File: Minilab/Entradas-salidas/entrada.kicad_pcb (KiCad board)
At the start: 2 copper layers, 140.6 x 50.8 mm, 82 parts, among them J1 Out 5V/0V, J10 Vin, J11 Vin, J12 Vin, J13 Vin, J15 Vin, J16 Vin, J17 VCC, J18 OUT, J19 GND, J2 Out 5V/0V, J20 Conn_01x08_Pin, J21 Conn_01x08_Pin, J3 Out 5V/0V, J4 Out 5V/0V, J5 Out 5V/0V, J6 Out 5V/0V, J7 Vin, J8 Vin, J9 Vin, SW1 SW_SPST, SW2 SW_SPST, SW3 SW_SPST, SW4 SW_SPST, SW5 SW_SPST, SW6 SW_SPST, U1 4049, U10 NE555P, U2 Mini360

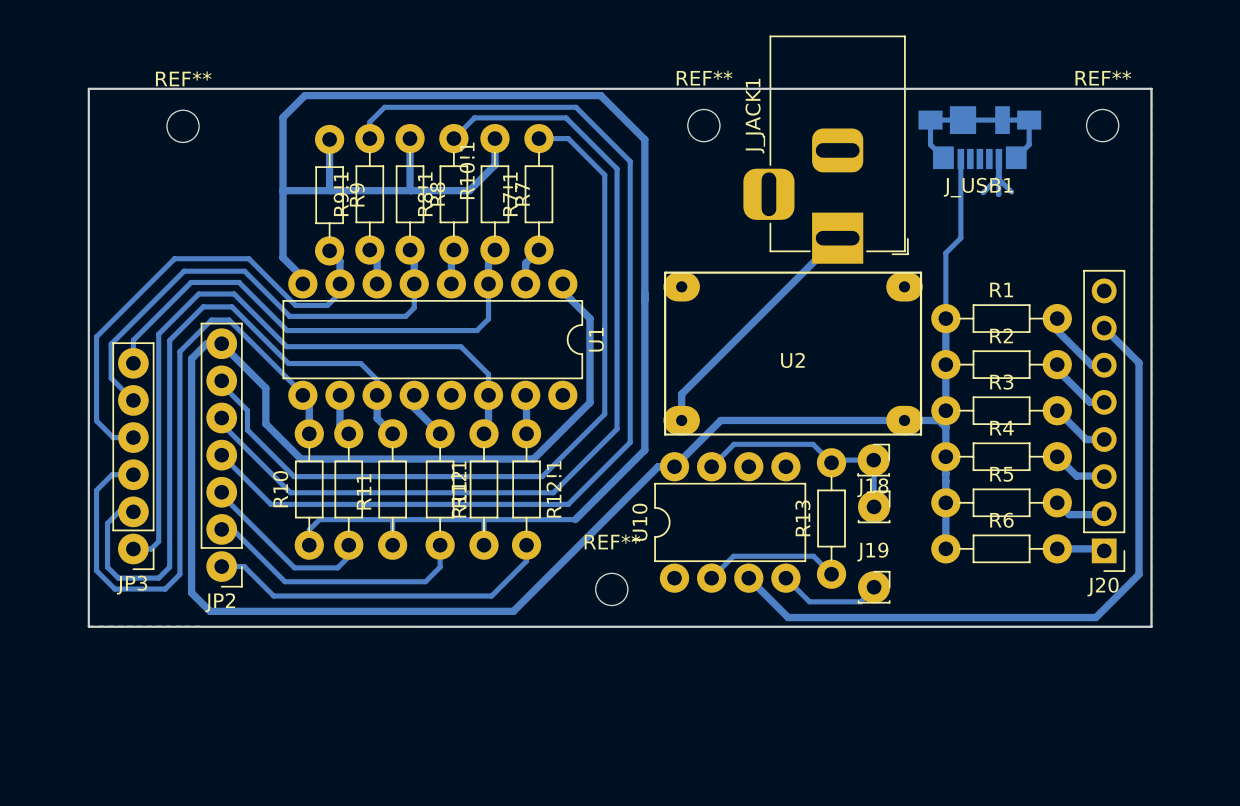
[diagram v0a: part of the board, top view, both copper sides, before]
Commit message: cambio oscilador
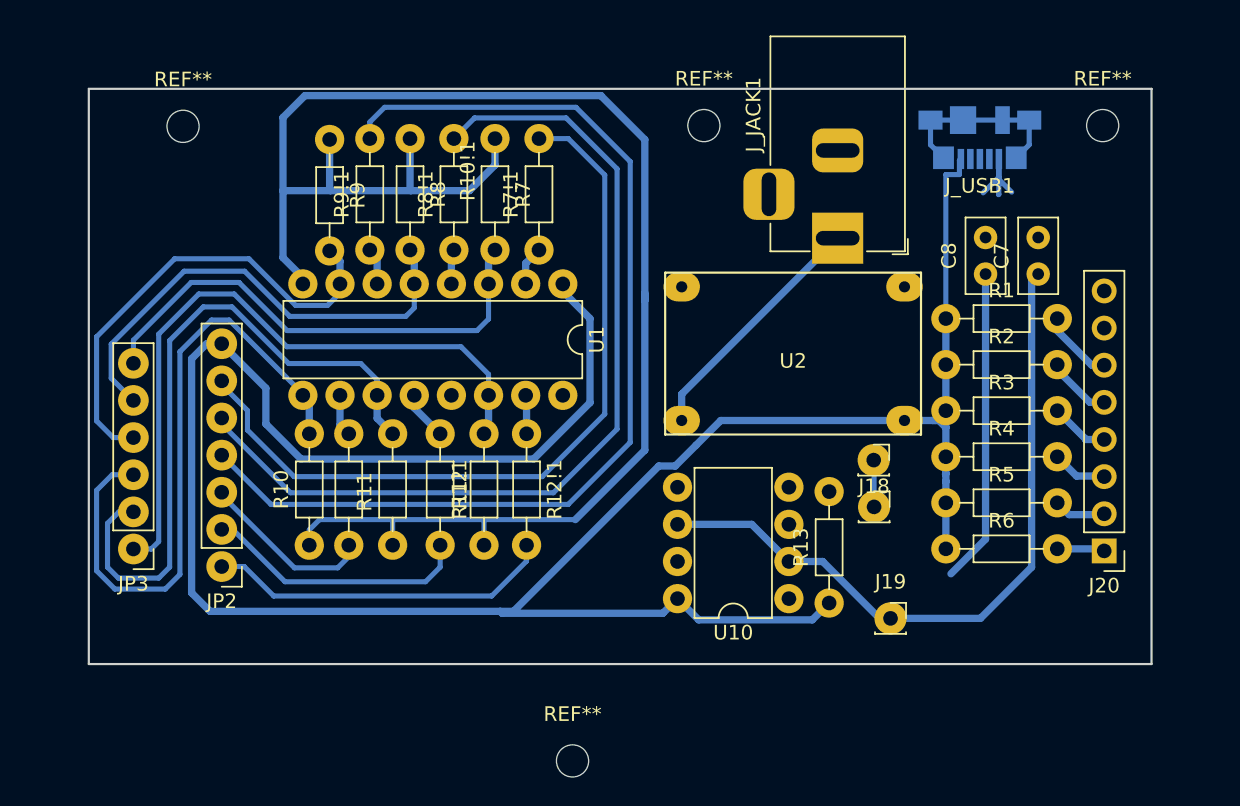
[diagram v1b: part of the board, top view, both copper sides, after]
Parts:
- added C7: 470nF, Capacitor_THT:C_Disc_D5.0mm_W2.5mm_P2.50mm, F.Cu at (228.6, 99.3)
- added C8: 10nF, Capacitor_THT:C_Disc_D5.0mm_W2.5mm_P2.50mm, F.Cu at (224.9, 99.3)
- moved REF** 12.0 mm to (196.7, 132.7)
- moved U10 7.95 mm to (211.5, 121.5), turned to 180 degrees
- moved J19 2.41 mm to (218.4, 122.9)
- moved R13 1.98 mm to (214.2, 121.8)
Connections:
- R13 pad 1: Net-(U10-TR) -> VCC
- U10 pad 2: Net-(U10-TR) -> /PinPot3
- U10 pad 4: /PinPot3 -> VCC
- U10 pad 5: unconnected-(U10-CV-Pad5) -> Net-(U10-CV)
- U10 pad 6: unconnected-(U10-THR-Pad6) -> /PinPot3
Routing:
- net /OscOut: track 46.9 -> 0.00 mm
- net /PinPot3: track 7.17 -> 48.6 mm
- net VCC: track 147.0 -> 171.5 mm
- net Net-(U10-CV): track 0.00 -> 21.5 mm
- net /PinPot1: track 16.6 -> 3.75 mm
- net Net-(U10-TR): track 9.33 -> 0.00 mm
- removed copper zone on B.Cu, net GND
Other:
- outline, holes or cut-outs redrawn

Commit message: listo para planchar
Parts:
- removed the REF** at (45.4, 17.3)
- removed the REF** at (96.1, 17.6)
- moved C7 74.2 mm to (155.7, 113.4), turned to 180 degrees
- moved C8 61.4 mm to (163.9, 105.4), turned to -90 degrees
- moved U10 59.4 mm to (153.1, 110.7), turned to 90 degrees
- moved REF** 52.8 mm to (147.3, 113.9)
- moved U2 51.1 mm to (161.7, 94.7)
- moved C6 50.8 mm to (206.1, 111.9)
- moved R10!1 50.8 mm to (131.6, 100.2)
- moved R11 50.8 mm to (134.6, 107.8)
- moved R11!1 50.8 mm to (137.9, 100.2)
- moved R12 50.8 mm to (140.9, 107.8)
- moved R7 50.8 mm to (141.6, 80.0)
- moved REF** 50.8 mm to (199.1, 118.1)
- moved REF** 50.8 mm to (199.1, 73.4)
- moved J10 50.8 mm to (92.7, 91.4)
- moved J11 50.8 mm to (92.7, 97.9)
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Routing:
- net GND: track 120.4 -> 196.7 mm
- net /OscOut: track 0.00 -> 73.5 mm
- net /PinPot3: track 48.6 -> 29.1 mm
- net Net-(U10-CV): track 21.5 -> 4.92 mm
- net /PinPot1: track 3.75 -> 19.3 mm
- net VCC: track 171.5 -> 162.8 mm
- net VCC_nreg: track 18.4 -> 20.7 mm
- net /PinR1: track 5.02 -> 4.07 mm
- added copper zone on B.Cu, net GND
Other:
- outline, holes or cut-outs redrawn

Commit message: update
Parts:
- removed the REF** at (183.2, 79.1)
- removed the REF** at (147.3, 113.9)
- removed the REF** at (120.3, 79.2)
- removed the REF** at (155.9, 79.1)
- added REF**: MountingHole_2.2mm_M2, MountingHole:MountingHole_2.2mm_M2, F.Cu at (119.5, 75.4)
- added REF**: MountingHole_2.2mm_M2, MountingHole:MountingHole_2.2mm_M2, F.Cu at (119.2, 104.8)
- added REF**: MountingHole_2.2mm_M2, MountingHole:MountingHole_2.2mm_M2, F.Cu at (154.3, 111.2)
- added REF**: MountingHole_2.2mm_M2, MountingHole:MountingHole_2.2mm_M2, F.Cu at (119.6, 138.3)
- J_USB1: footprint Connector_USB:USB_Micro-B_Molex_47346-0001 -> minilab:usb
- moved J_USB1 54.5 mm to (120.5, 83.9), turned to 90 degrees
- moved R9 49.2 mm to (120.5, 128.3), turned to 0 degrees
- moved J20 47.8 mm to (148.6, 75.3), turned to -90 degrees
- moved JP3 46.1 mm to (148.5, 141.7), turned to -90 degrees
- moved R8 45.5 mm to (120.4, 122.8), turned to 0 degrees
- moved R7 42.6 mm to (120.4, 117.0), turned to 0 degrees
- moved R1 39.4 mm to (133.8, 86.1), turned to 90 degrees
- moved J_JACK1 38.8 mm to (127.2, 95.1), turned to 0 degrees
- moved R9!1 38.2 mm to (128.0, 125.5), turned to 180 degrees
- moved JP2 37.6 mm to (149.7, 135.6), turned to -90 degrees
- moved R2 37.1 mm to (136.9, 86.1), turned to 90 degrees
- moved C1 36.8 mm to (169.8, 85.6)
- moved C2 36.8 mm to (169.8, 92.1)
- moved C3 36.8 mm to (169.8, 98.6)
- moved C4 36.8 mm to (169.8, 105.1)
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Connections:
- J_USB1 pad 2: unconnected-(J_USB1-D--Pad2) -> VCC
- J_USB1 pad 4: unconnected-(J_USB1-ID-Pad4) -> GND
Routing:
- net GND: track 196.7 -> 240.4 mm, vias 0 -> 2
- net unconnected-(J_USB1-Shield-Pad6): track 12.6 -> 0.00 mm
- net VCC_nreg: track 20.7 -> 18.4 mm
- net /PinPot3: track 29.1 -> 30.6 mm
- net VCC: track 162.8 -> 161.5 mm
- net /PinBIn: track 33.8 -> 34.8 mm
- net /PinDIn: track 45.7 -> 46.4 mm
- net /PinAIn: track 34.1 -> 34.6 mm
- removed copper zone on B.Cu, net (none)
- removed copper zone on B.Cu, net GND
- removed copper zone on B.Cu, net GNDSw
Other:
- board size 140.6 x 50.8 mm -> 97.7 x 72.7 mm
